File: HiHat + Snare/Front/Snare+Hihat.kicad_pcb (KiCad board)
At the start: 2 copper layers, 40 x 133 mm, 4 parts

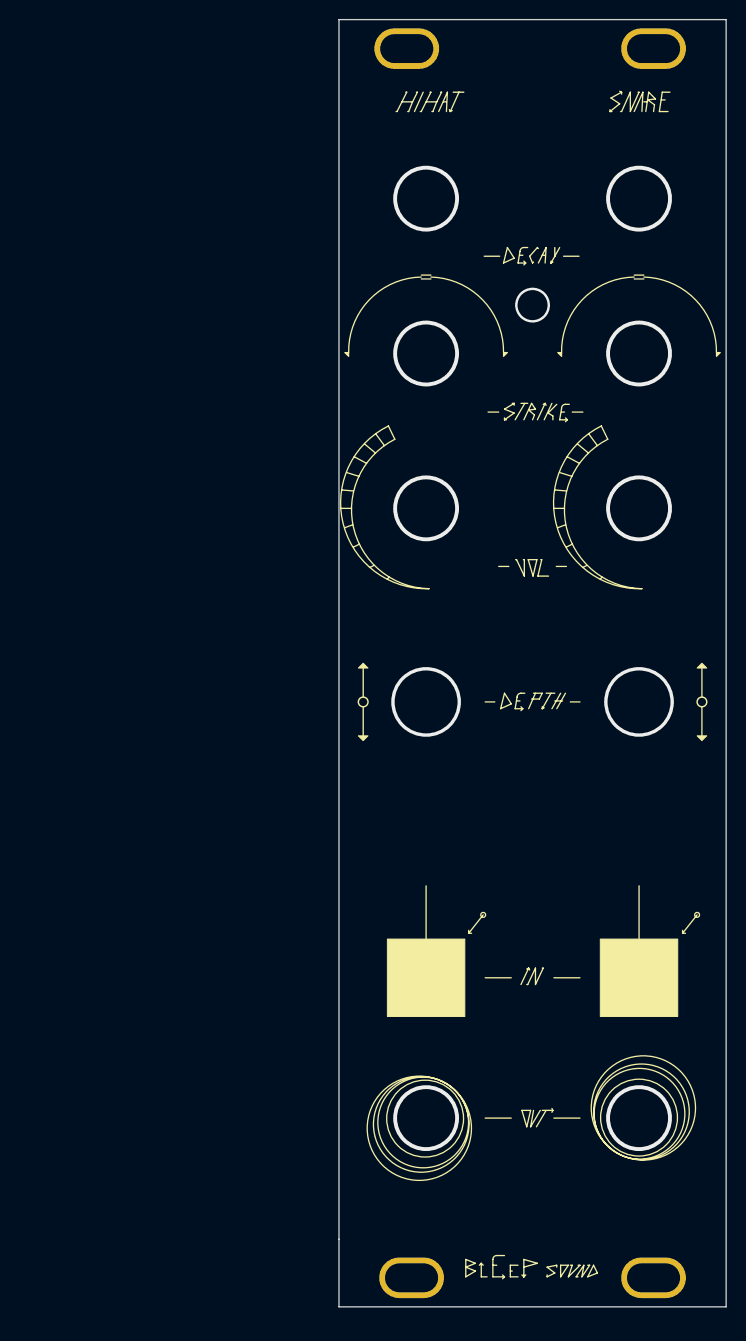
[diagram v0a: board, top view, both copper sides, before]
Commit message: Update front panel and jack board for better handling
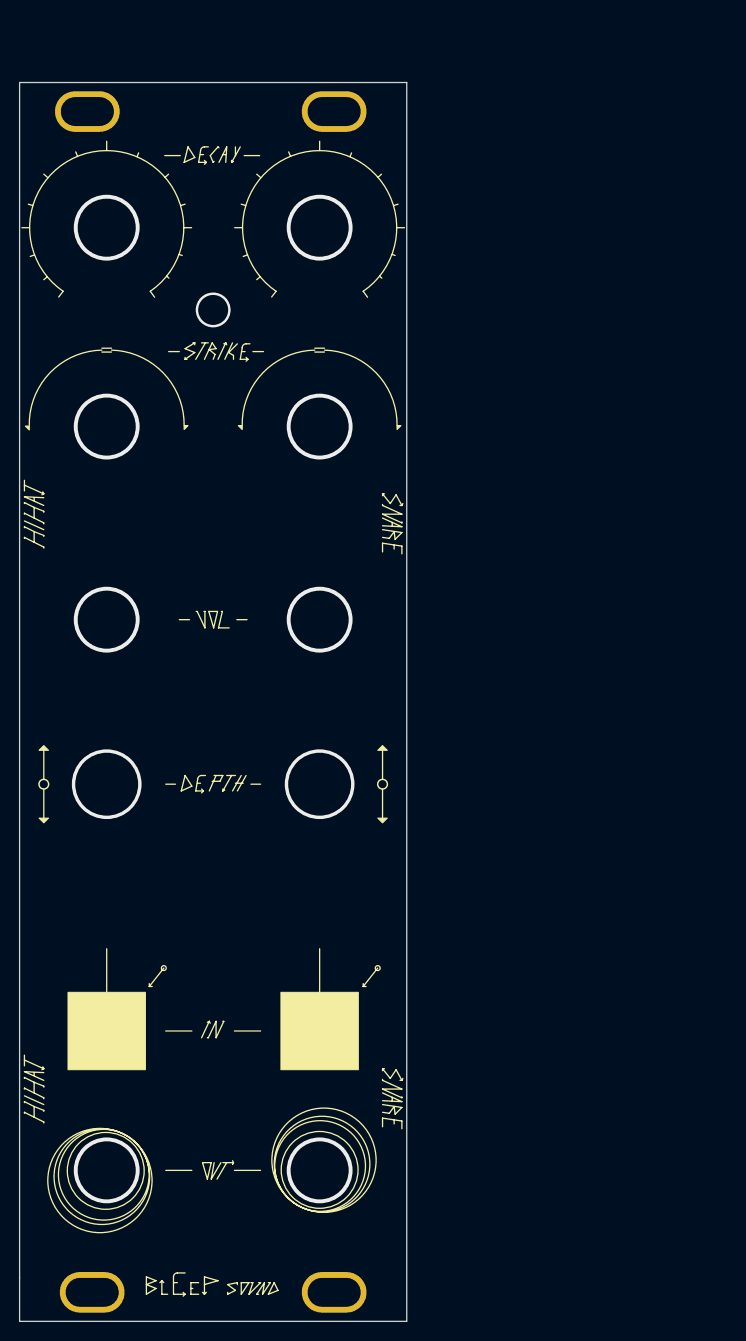
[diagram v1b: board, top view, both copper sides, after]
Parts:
- removed the REF** at (150.0, 149.5)
- removed the REF** at (124.5, 22.5)
- removed the REF** at (150.0, 22.5)
- removed the REF** at (125.0, 149.5)
- added REF**: Doepfer Mounting hole, Synth:Doepfer Mounting hole, F.Cu at (91.5, 29.0)
- added REF**: Doepfer Mounting hole, Synth:Doepfer Mounting hole, F.Cu at (117.0, 151.0)
- added REF**: Doepfer Mounting hole, Synth:Doepfer Mounting hole, F.Cu at (117.0, 29.0)
- added REF**: Doepfer Mounting hole, Synth:Doepfer Mounting hole, F.Cu at (92.0, 151.0)
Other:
- board size 40 x 133 mm -> 40 x 128 mm
